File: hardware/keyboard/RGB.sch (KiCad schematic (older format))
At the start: 12 parts, among them U1 IS31FL3733-QF, U2 IS31FL3733-QF

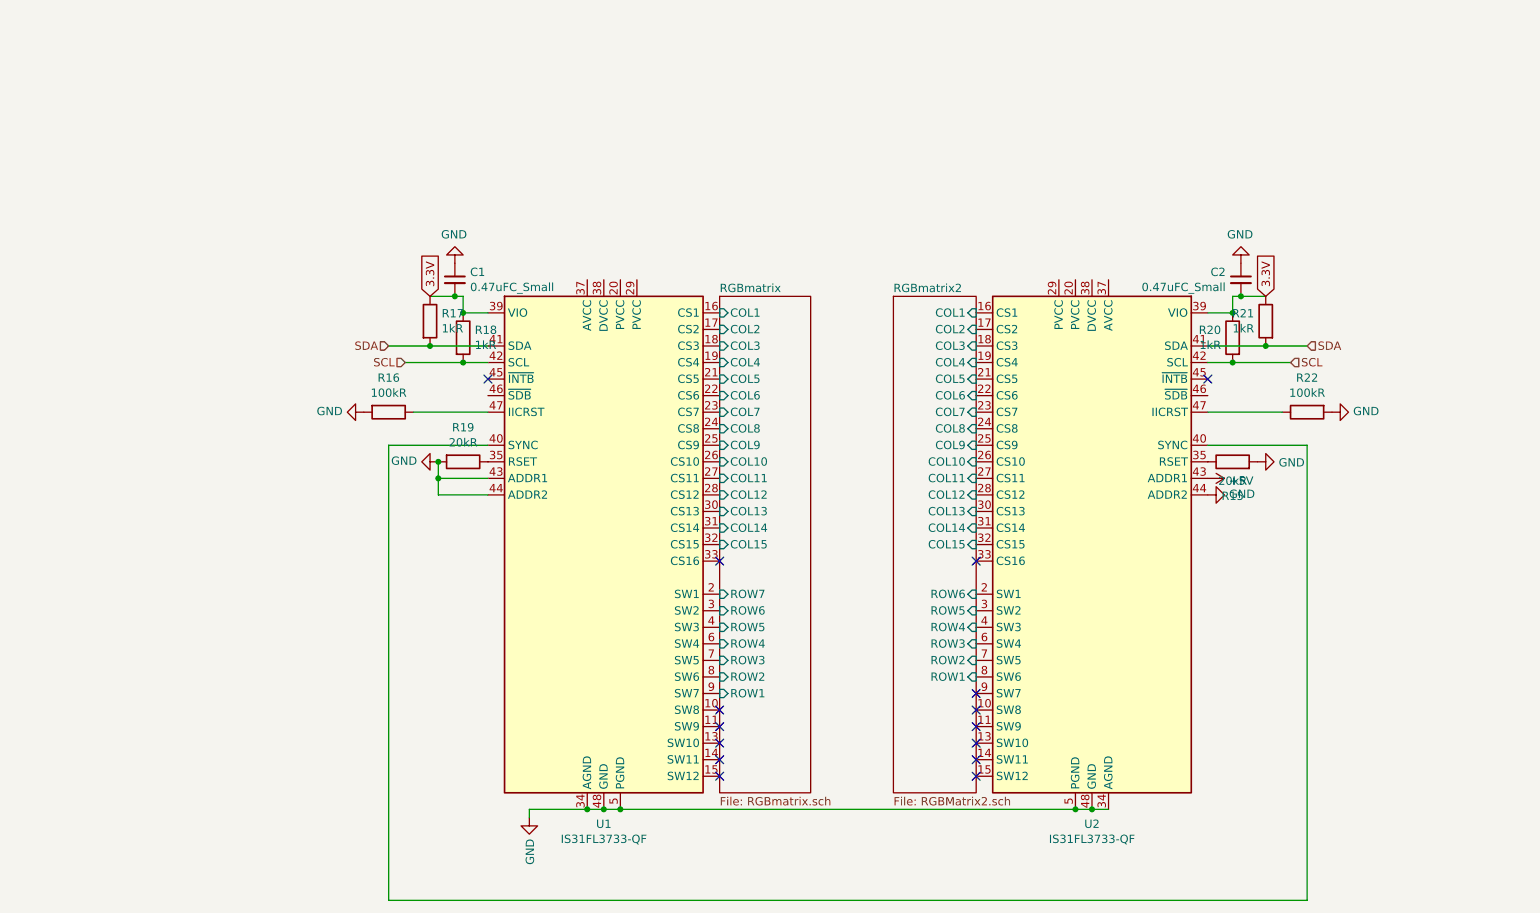
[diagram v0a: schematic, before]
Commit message: switch to proper type of RGB(Common anode)
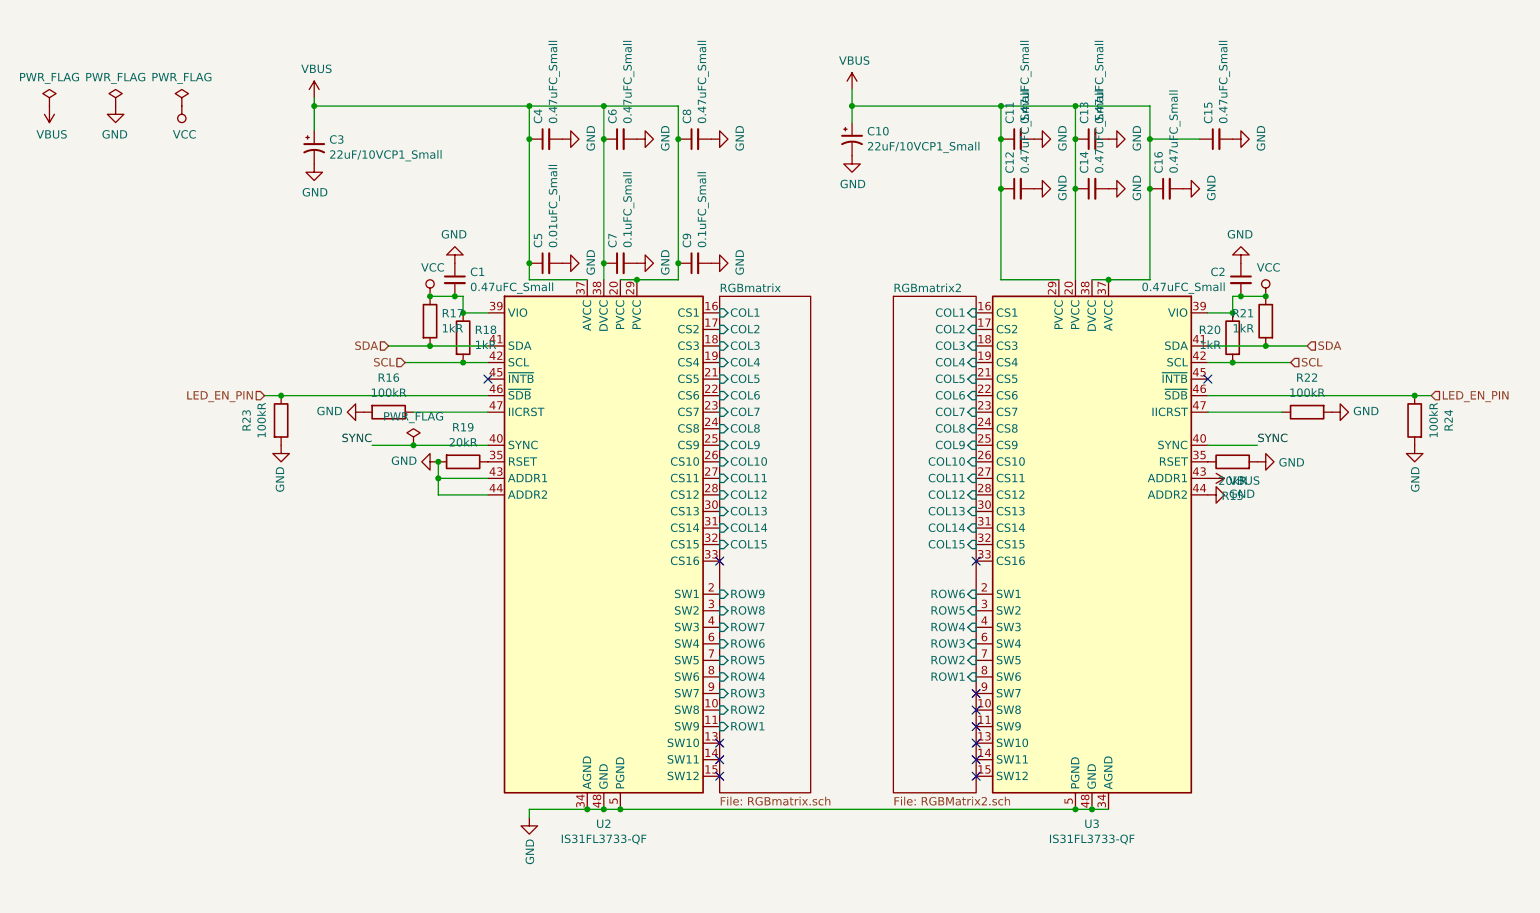
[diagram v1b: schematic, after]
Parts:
- added C10, C3: 22uF/10VCP1_Small, symbol Device:CP1_Small
- added C11, C12, C13, C14, C15, C16, C4, C6, C8: 0.47uFC_Small, symbol Device:C_Small
- added C5: 0.01uFC_Small, symbol Device:C_Small
- added C7, C9: 0.1uFC_Small, symbol Device:C_Small
- added R23, R24: 100kR, symbol Device:R
- renumbered U1 to U2, U2 to U3
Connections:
- net +5V is gone; now on net VBUS: U3.43 (ADDR1)
- net GND: now also C10.2, C11.2, C12.2, C13.2, C14.2, C15.2, C16.2, C3.2, C4.2, C5.2, C6.2, C7.2, C8.2, C9.2, R23.2, R24.2
- net RGBmatrix/ROW1: now also U2.11 (SW9); no longer U2.9 (SW7)
- net RGBmatrix/ROW2: now also U2.10 (SW8); no longer U2.8 (SW6)
- net RGBmatrix/ROW3: now also U2.9 (SW7); no longer U2.7 (SW5)
- net RGBmatrix/ROW4: now also U2.8 (SW6); no longer U2.6 (SW4)
- net RGBmatrix/ROW5: now also U2.7 (SW5); no longer U2.4 (SW3)
- net RGBmatrix/ROW6: now also U2.6 (SW4); no longer U2.3 (SW2)
- net RGBmatrix/ROW7: now also U2.4 (SW3); no longer U2.2 (SW1)
- net VBUS: now reaches U3.20 (PVCC)
- net VBUS: now also U2.20 (PVCC), U2.29 (PVCC), U2.37 (AVCC), U2.38 (DVCC), U3.29 (PVCC), U3.37 (AVCC), U3.38 (DVCC), C10.1, C11.1, C12.1, C13.1, C14.1, C15.1, C16.1, C3.1, C4.1, C5.1, C6.1, C7.1, C8.1, C9.1
- net SYNC: now reaches U2.40 (SYNC), U3.40 (SYNC)
- net LED_EN_PIN: now reaches U3.46 (~SDB)
- net LED_EN_PIN: now also U2.46 (~SDB), R23.1, R24.1
- net 3.3V renamed VCC
- new net RGBmatrix/ROW8: U2.3 (SW2)
- new net RGBmatrix/ROW9: U2.2 (SW1)
- no-connect marks 15 -> 13

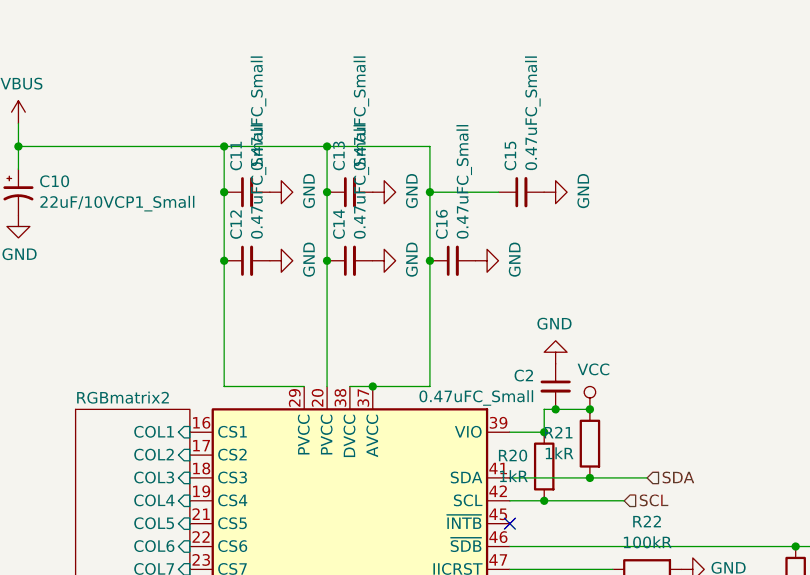
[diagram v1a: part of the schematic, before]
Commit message: Use proper capacitors
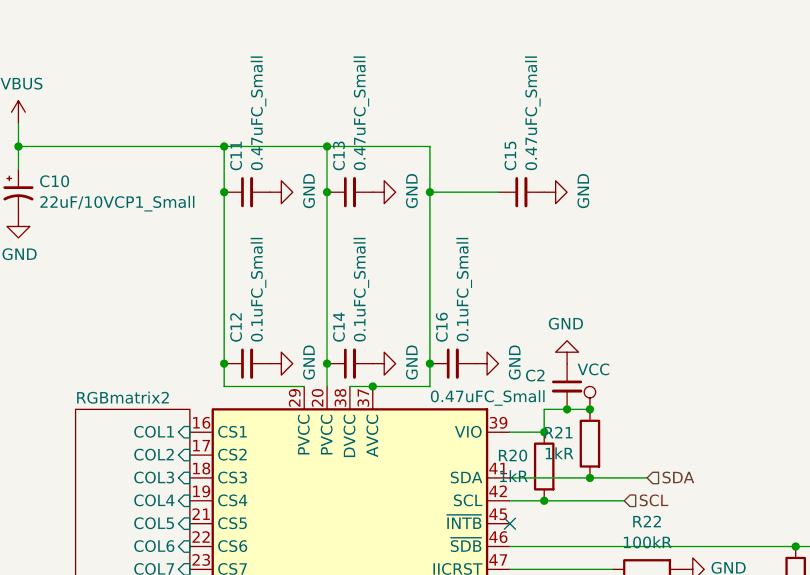
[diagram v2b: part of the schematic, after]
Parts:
- C12, C14, C16: value 0.47uFC_Small -> 0.1uFC_Small
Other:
- moved on the sheet: C12, C14, C16, C2
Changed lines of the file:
@@
 L power:GND #PWR010
 U 1 1 5E42518F
-P 8000 1900
-F 0 "#PWR010" H 8000 1650 50  0001 C CNN
-F 1 "GND" H 8005 1727 50  0000 C CNN
-F 2 "" H 8000 1900 50  0001 C CNN
-F 3 "" H 8000 1900 50  0001 C CNN
-	1    8000 1900
+P 8050 1900
+F 0 "#PWR010" H 8050 1650 50  0001 C CNN
+F 1 "GND" H 8055 1727 50  0000 C CNN
+F 2 "" H 8050 1900 50  0001 C CNN
+F 3 "" H 8050 1900 50  0001 C CNN
+	1    8050 1900
 	-1   0    0    1
 $EndComp
@@
 	0    -1   1    0
 $EndComp
-Wire Wire Line
-	8000 2100 7950 2100
-Connection ~ 8000 2100
 $Comp
 L Device:C_Small C2
 U 1 1 5E406F19
-P 8000 2000
-F 0 "C2" H 8092 2046 50  0000 L CNN
-F 1 "0.47uFC_Small" H 8092 1955 50  0000 L CNN
-F 2 "" H 8000 2000 50  0001 C CNN
-F 3 "~" H 8000 2000 50  0001 C CNN
-	1    8000 2000
+P 8050 2000
+F 0 "C2" H 8142 2046 50  0000 L CNN
+F 1 "0.47uFC_Small" H 8142 1955 50  0000 L CNN
+F 2 "" H 8050 2000 50  0001 C CNN
+F 3 "~" H 8050 2000 50  0001 C CNN
+	1    8050 2000
 	-1   0    0    -1
 $EndComp
@@
 	7950 2100 7950 2200
 Wire Wire Line
-	8150 2100 8000 2100
+	8150 2100 8050 2100
 Wire Wire Line
 	7950 2500 8300 2500
@@
 L Device:C_Small C14
 U 1 1 5E45A529
-P 7100 1450
-F 0 "C14" H 7192 1496 50  0000 L CNN
-F 1 "0.47uFC_Small" H 7192 1405 50  0000 L CNN
-F 2 "" H 7100 1450 50  0001 C CNN
-F 3 "~" H 7100 1450 50  0001 C CNN
-	1    7100 1450
+P 7100 1900
+F 0 "C14" H 7192 1946 50  0000 L CNN
+F 1 "0.1uFC_Small" H 7192 1855 50  0000 L CNN
+F 2 "" H 7100 1900 50  0001 C CNN
+F 3 "~" H 7100 1900 50  0001 C CNN
+	1    7100 1900
 	0    -1   -1   0
 $EndComp
@@
 L power:GND #PWR0101
 U 1 1 5E45ABD9
-P 7200 1450
-F 0 "#PWR0101" H 7200 1200 50  0001 C CNN
-F 1 "GND" H 7205 1277 50  0000 C CNN
-F 2 "" H 7200 1450 50  0001 C CNN
-F 3 "" H 7200 1450 50  0001 C CNN
-	1    7200 1450
+P 7200 1900
+F 0 "#PWR0101" H 7200 1650 50  0001 C CNN
+F 1 "GND" H 7205 1727 50  0000 C CNN
+F 2 "" H 7200 1900 50  0001 C CNN
+F 3 "" H 7200 1900 50  0001 C CNN
+	1    7200 1900
 	0    -1   -1   0
 $EndComp
@@
 L Device:C_Small C12
 U 1 1 5E45C9C4
-P 6650 1450
-F 0 "C12" H 6742 1496 50  0000 L CNN
-F 1 "0.47uFC_Small" H 6742 1405 50  0000 L CNN
-F 2 "" H 6650 1450 50  0001 C CNN
-F 3 "~" H 6650 1450 50  0001 C CNN
-	1    6650 1450
+P 6650 1900
+F 0 "C12" H 6742 1946 50  0000 L CNN
+F 1 "0.1uFC_Small" H 6742 1855 50  0000 L CNN
+F 2 "" H 6650 1900 50  0001 C CNN
+F 3 "~" H 6650 1900 50  0001 C CNN
+	1    6650 1900
 	0    -1   -1   0
 $EndComp
@@
 L power:GND #PWR0103
 U 1 1 5E45C9CA
-P 6750 1450
-F 0 "#PWR0103" H 6750 1200 50  0001 C CNN
-F 1 "GND" H 6755 1277 50  0000 C CNN
-F 2 "" H 6750 1450 50  0001 C CNN
-F 3 "" H 6750 1450 50  0001 C CNN
-	1    6750 1450
+P 6750 1900
+F 0 "#PWR0103" H 6750 1650 50  0001 C CNN
+F 1 "GND" H 6755 1727 50  0000 C CNN
+F 2 "" H 6750 1900 50  0001 C CNN
+F 3 "" H 6750 1900 50  0001 C CNN
+	1    6750 1900
 	0    -1   -1   0
 $EndComp
@@
 L Device:C_Small C16
 U 1 1 5E45E090
-P 7550 1450
-F 0 "C16" H 7642 1496 50  0000 L CNN
-F 1 "0.47uFC_Small" H 7642 1405 50  0000 L CNN
-F 2 "" H 7550 1450 50  0001 C CNN
-F 3 "~" H 7550 1450 50  0001 C CNN
-	1    7550 1450
+P 7550 1900
+F 0 "C16" H 7642 1946 50  0000 L CNN
+F 1 "0.1uFC_Small" H 7642 1855 50  0000 L CNN
+F 2 "" H 7550 1900 50  0001 C CNN
+F 3 "~" H 7550 1900 50  0001 C CNN
+	1    7550 1900
 	0    -1   -1   0
 $EndComp
@@
 L power:GND #PWR0105
 U 1 1 5E45E096
-P 7650 1450
-F 0 "#PWR0105" H 7650 1200 50  0001 C CNN
-F 1 "GND" H 7655 1277 50  0000 C CNN
-F 2 "" H 7650 1450 50  0001 C CNN
-F 3 "" H 7650 1450 50  0001 C CNN
-	1    7650 1450
+P 7650 1900
+F 0 "#PWR0105" H 7650 1650 50  0001 C CNN
+F 1 "GND" H 7655 1727 50  0000 C CNN
+F 2 "" H 7650 1900 50  0001 C CNN
+F 3 "" H 7650 1900 50  0001 C CNN
+	1    7650 1900
 	0    -1   -1   0
 $EndComp
@@
 	7100 2000 7200 2000
 Wire Wire Line
-	7450 1450 7450 2000
-Wire Wire Line
 	7450 2000 7200 2000
-Connection ~ 7450 1450
 Connection ~ 7200 2000
 Wire Wire Line
-	7000 1150 7000 1450
-Connection ~ 7000 1450
-Wire Wire Line
-	7000 1450 7000 2000
-Wire Wire Line
-	6550 1150 6550 1450
-Wire Wire Line
-	6550 1450 6550 2000
-Wire Wire Line
 	6550 2000 6900 2000
-Connection ~ 6550 1450
 Wire Wire Line
 	7450 950  7000 950
@@
 	7750 1150 7450 1150
 Connection ~ 7450 1150
-Wire Wire Line
-	7450 1150 7450 1450
 Connection ~ 3700 1900
 Wire Wire Line
@@
 	1    0    0    1
 $EndComp
+Connection ~ 6550 1900
+Wire Wire Line
+	6550 1900 6550 2000
+Wire Wire Line
+	6550 1150 6550 1900
+Connection ~ 7000 1900
+Wire Wire Line
+	7000 1900 7000 2000
+Wire Wire Line
+	7000 1150 7000 1900
+Connection ~ 7450 1900
+Wire Wire Line
+	7450 1900 7450 2000
+Wire Wire Line
+	7450 1150 7450 1900
+Connection ~ 8050 2100
+Wire Wire Line
+	7950 2100 8050 2100
 $EndSCHEMATC

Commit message: fix unconnected rgb
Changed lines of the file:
@@
 Wire Wire Line
 	4600 1150 4600 1900
-$Comp
-L power:PWR_FLAG #FLG0101
-U 1 1 5E10BE47
-P 1200 950
-F 0 "#FLG0101" H 1200 1025 50  0001 C CNN
-F 1 "PWR_FLAG" H 1200 1123 50  0000 C CNN
-F 2 "" H 1200 950 50  0001 C CNN
-F 3 "~" H 1200 950 50  0001 C CNN
-	1    1200 950
-	1    0    0    -1
-$EndComp
-$Comp
-L power:PWR_FLAG #FLG0102
-U 1 1 5E10C6CD
-P 800 950
-F 0 "#FLG0102" H 800 1025 50  0001 C CNN
-F 1 "PWR_FLAG" H 800 1123 50  0000 C CNN
-F 2 "" H 800 950 50  0001 C CNN
-F 3 "~" H 800 950 50  0001 C CNN
-	1    800  950
-	1    0    0    -1
-$EndComp
 Wire Wire Line
 	2400 950  3700 950
-$Comp
-L power:VBUS #PWR0127
-U 1 1 5E11485A
-P 800 950
-F 0 "#PWR0127" H 800 800 50  0001 C CNN
-F 1 "VBUS" H 815 1123 50  0000 C CNN
-F 2 "" H 800 950 50  0001 C CNN
-F 3 "" H 800 950 50  0001 C CNN
-	1    800  950
-	1    0    0    1
-$EndComp
-$Comp
-L power:GND #PWR0128
-U 1 1 5E119246
-P 1200 950
-F 0 "#PWR0128" H 1200 700 50  0001 C CNN
-F 1 "GND" H 1205 777 50  0000 C CNN
-F 2 "" H 1200 950 50  0001 C CNN
-F 3 "" H 1200 950 50  0001 C CNN
-	1    1200 950
-	-1   0    0    -1
-$EndComp
-$Comp
-L power:PWR_FLAG #FLG0103
-U 1 1 5E11267C
-P 1600 950
-F 0 "#FLG0103" H 1600 1025 50  0001 C CNN
-F 1 "PWR_FLAG" H 1600 1123 50  0000 C CNN
-F 2 "" H 1600 950 50  0001 C CNN
-F 3 "~" H 1600 950 50  0001 C CNN
-	1    1600 950
-	1    0    0    -1
-$EndComp
-$Comp
-L power:VCC #PWR0129
-U 1 1 5E11DE90
-P 1600 950
-F 0 "#PWR0129" H 1600 800 50  0001 C CNN
-F 1 "VCC" H 1617 1123 50  0000 C CNN
-F 2 "" H 1600 950 50  0001 C CNN
-F 3 "" H 1600 950 50  0001 C CNN
-	1    1600 950
-	1    0    0    1
-$EndComp
 Connection ~ 6550 1900
 Wire Wire Line
